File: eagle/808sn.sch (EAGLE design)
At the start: 76 parts, among them IC1 TL072P, IC2 TL072P, Q1 2N3704, Q45 BC546A, Q46 BC556, Q47 BC546A, Q48 BC546A, Q49 BC546A

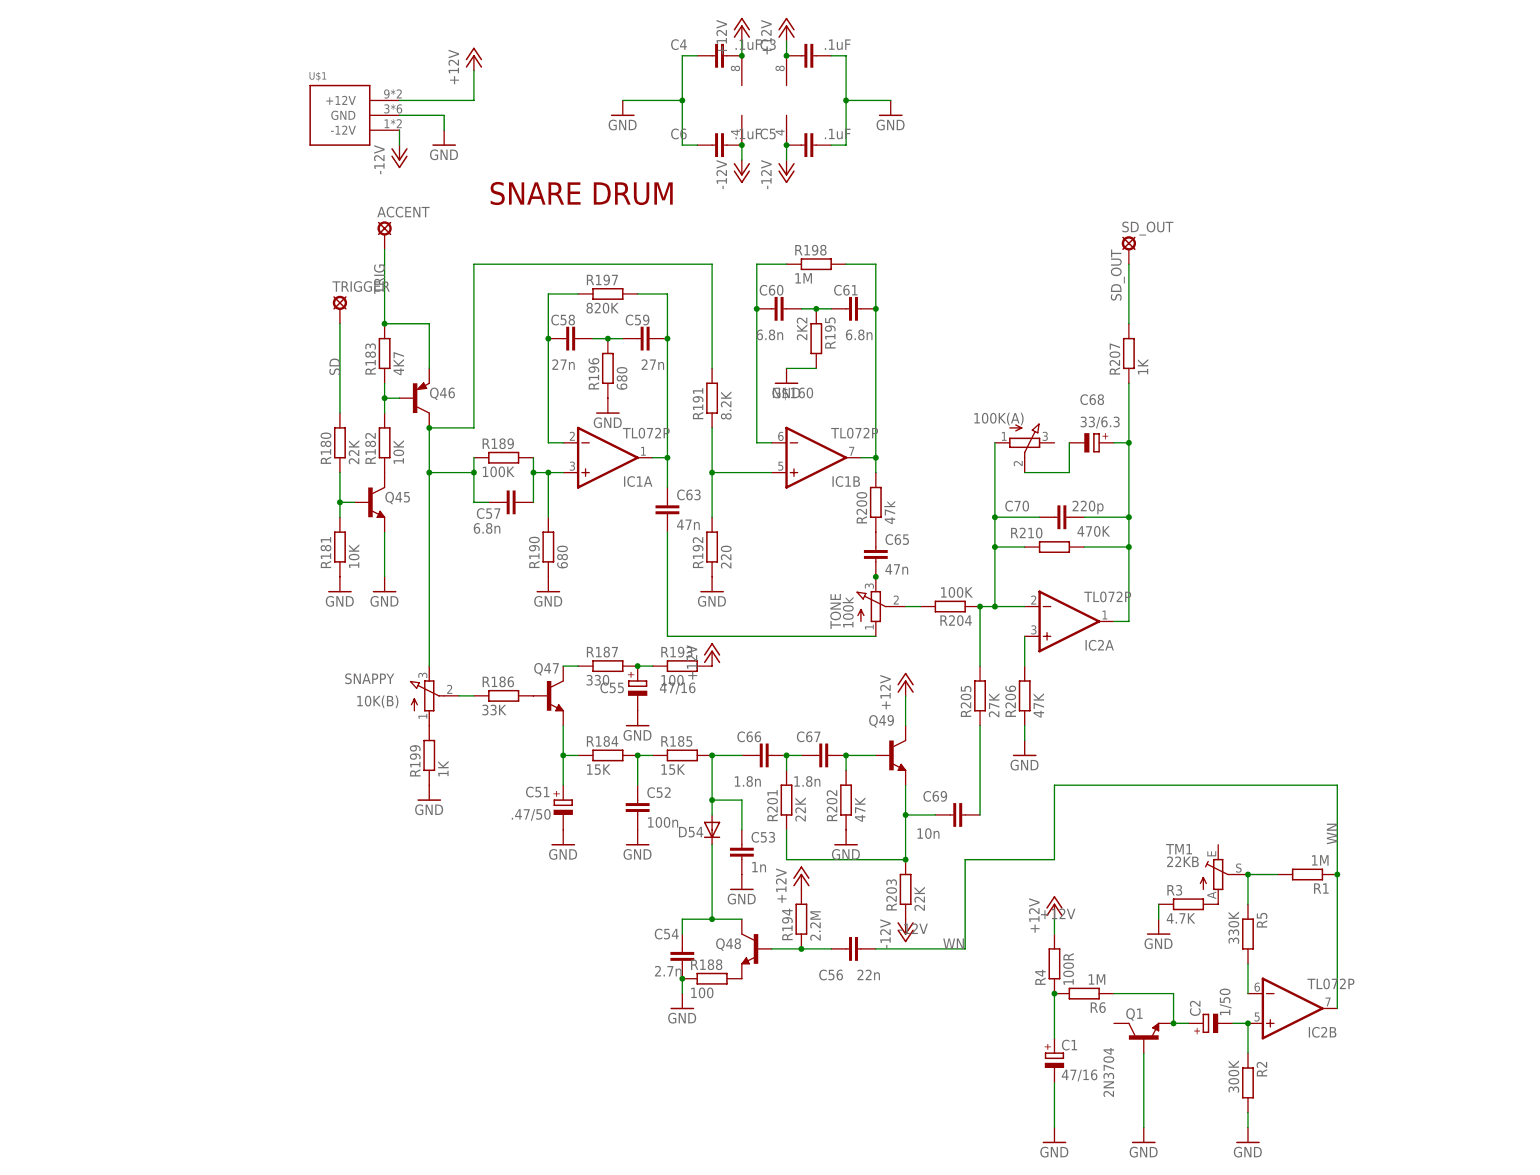
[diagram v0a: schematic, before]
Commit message: updated fittings and replaced with 2n390x
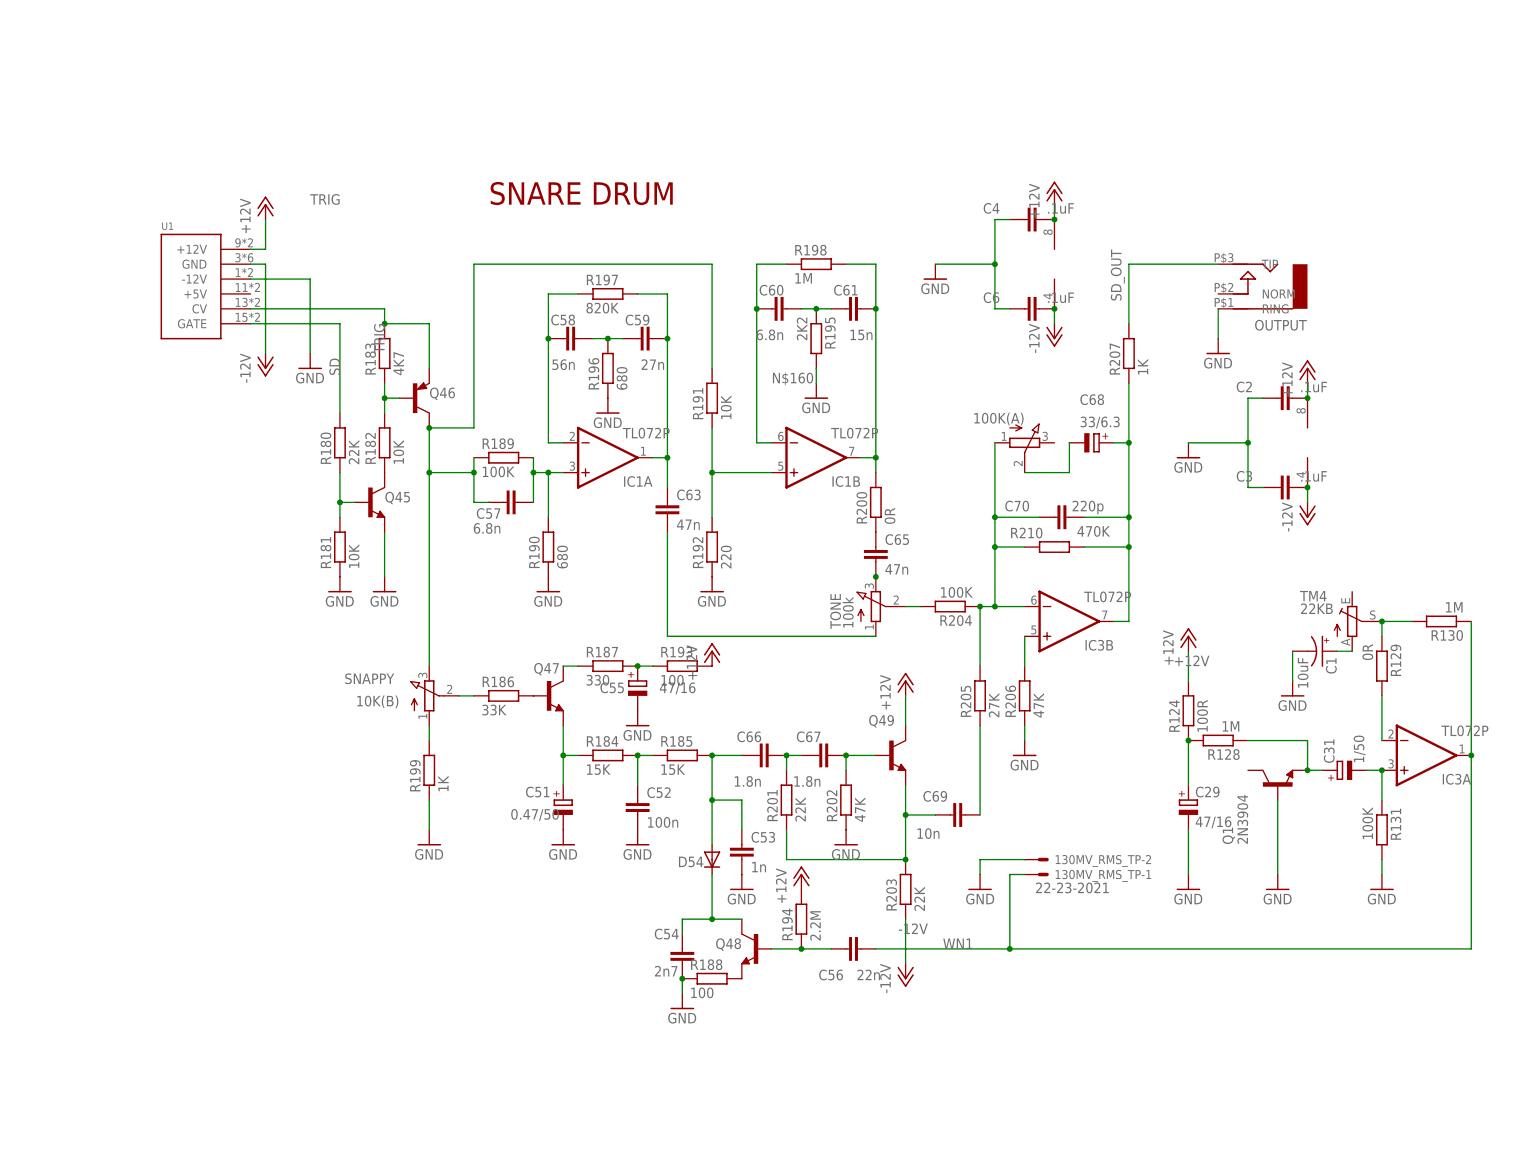
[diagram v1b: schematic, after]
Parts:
- removed ACCENT, SD_OUT, TRIGGER: LSP11, solpad:LSP11
- removed C5: .1uF, TR808clone:C-EU025-025X050
- removed IC2: TL072P, linear:TL072P
- removed R1, R6: 1M, TR808clone:R-EU_0207/5V
- removed R2: 300K, TR808clone:R-EU_0207/5V
- removed R3: 4.7K, TR808clone:R-EU_0207/5V
- removed R4: 100R, TR808clone:R-EU_0207/5V
- removed R5: 330K, TR808clone:R-EU_0207/5V
- removed TM1: 22KB, pot:TRIM_1234-S64YW
- removed U$1: POWER_SIMPLE10, eurorack:POWER_SIMPLE10
- added 130MV_RMS_TP: 22-23-2021, con-molex:22-23-2021
- added C29: 47/16, TR808clone:CPOL-EUE2.5-5
- added C31: 1/50, TR808clone:CPOL-EUE2.5-5
- added IC3: TL072P, linear:TL072P
- added OUTPUT: AUDIO-JACK, erthenvar:AUDIO-JACK
- added R124: 100R, TR808clone:R-EU_0207/7
- added R128, R130: 1M, TR808clone:R-EU_0207/7
- added R129: 0R, TR808clone:R-EU_0207/7
- added R131: 100K, TR808clone:R-EU_0207/7
- added TM4: 22KB, TR808clone:TRIM_EU-B64Y
- added U1: POWER, eurorack:POWER
- C1: value 47/16 -> 10uF; device TR808clone:CPOL-EUE2.5-5 -> rcl:CPOL-USB45181A
- C2: value 1/50 -> .1uF; device TR808clone:CPOL-EUE2.5-5 -> TR808clone:C-EU025-025X050
- C51: value .47/50 -> 0.47/50
- C54: value 2.7n -> 2n7
- C58: value 27n -> 56n
- C61: value 6.8n -> 15n
- Q1: value 2N3704 -> 2N3904; device transistor:2N3704 -> transistor-npn:2N3904
- Q45, Q47, Q48, Q49: value BC546A -> 2N3904; device transistor-npn:BC546A -> 808_lt:2N3904
- Q46: value BC556 -> 2N3906; device transistor-pnp:BC556 -> 808_lt:2N3906
- R191: value 8.2K -> 10K
- R200: value 47k -> 0R
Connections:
- removed net N$2: C2.-, IC2B.+IN, R2.1
- removed net N$707: R1.2, R5.1, TM1.S
- removed net N$709: C2.+, Q1.E, R6.1
- removed net N$710: C1.+, R4.1, R6.2
- removed net N$711: R3.2, TM1.A
- removed net WN: C56.2, IC2B.OUT, R1.1
- new net N$280: C31.-, IC3A.+IN, R131.1
- new net N$4: IC3A.-IN, R129.2
- new net N$490: R129.1, R130.2, TM4.S
- new net N$491: C31.+, Q1.E, R128.1
- new net N$492: C29.+, R124.1, R128.2
- new net WN1: 130MV_RMS_TP-1.S, C56.2, IC3A.OUT, R130.1
- net +12V: now also C2.2, IC3P.V+, R124.2, U1.+12V; no longer C3.1, IC2P.V+, R4.2, U$1.+12V
- net -12V: now also C3.2, IC3P.V-, U1.GND; no longer C5.1, IC2P.V-, U$1.-12V
- net GND: now also 130MV_RMS_TP-2.S, C2.1, C29.-, C3.1, OUTPUT.RING, R131.2, U1.-12V; no longer C3.2, C5.2, R2.2, R3.1, U$1.GND
- net N$1: now also IC3B.+IN; no longer IC2A.+IN
- net N$129: now also IC3B.OUT; no longer IC2A.OUT
- net N$3: now also C1.+, TM4.A; no longer IC2B.-IN, R5.2
- net N$35: now also IC3B.-IN; no longer IC2A.-IN
- net SD: now also U1.GATE; no longer TRIGGER.MP
- net SD_OUT: now also OUTPUT.TIP; no longer SD_OUT.MP
- net TRIG: now also U1.CV; no longer ACCENT.MP
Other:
- moved on the sheet: C1, C3, C4, C6, D54, R199

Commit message: 92pct autorouted
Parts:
- removed U1: POWER, eurorack:POWER
- added ACCENT, GATE: LSP10, solpad:LSP10
- added C5, C7: 10u, rcl:CPOL-USB45181A
- added OUTPUT_NORM: 22-23-2021, con-molex:22-23-2021
- added PWR1: POWER, eurorack:POWER
- added U$1, U$2: FB, adafruit:FB
- R187, R193, R195, R196, R201, R205: device TR808clone:R-EU_0207/5V -> TR808clone:R-EU_0207/7
- R194, R203, R207: device TR808clone:R-EU_0207/5V -> TR808clone:R-EU_0309/10
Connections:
- new net N$10: PWR1.+12V, U$1.1
- new net N$2: OUTPUT.NORM, OUTPUT_NORM-1.S
- new net N$37: PWR1.-12V, U$2.1
- net +12V: now also C5.+, U$1.2; no longer U1.+12V
- net -12V: now also C7.-, U$2.2; no longer U1.GND
- net GND: now also OUTPUT_NORM-2.S; no longer U1.-12V
- net N$26: now also C5.-, C7.+, PWR1.GND
- net SD: now also GATE.MP, PWR1.GATE; no longer U1.GATE
- net TRIG: now also ACCENT.MP, PWR1.CV; no longer U1.CV
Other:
- moved on the sheet: C2, C3, OUTPUT, R207

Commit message: board started over
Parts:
- C52: device TR808clone:C-EU075-032X103 -> TR808clone:C-EU050-045X075
- C6: device TR808clone:C-EU025-025X050 -> TR808clone:C-EU050-025X075
- C69: device TR808clone:C-EU3.5MM_PITCH -> TR808clone:C-EU075-042X103
- R194, R203: device TR808clone:R-EU_0309/10 -> TR808clone:R-EU_0207/7
- R204: device TR808clone:R-EU_0207/5V -> TR808clone:R-EU_0207/7
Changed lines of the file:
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@@
 <part name="R184" library="TR808clone" deviceset="R-EU_" device="0207/5V" value="15K"/>
 <part name="R185" library="TR808clone" deviceset="R-EU_" device="0207/5V" value="15K"/>
-<part name="C52" library="TR808clone" deviceset="C-EU" device="075-032X103" value="100n"/>
+<part name="C52" library="TR808clone" deviceset="C-EU" device="050-045X075" value="100n"/>
 <part name="C55" library="TR808clone" deviceset="CPOL-EU" device="E2-5" value="47/16"/>
 <part name="C51" library="TR808clone" deviceset="CPOL-EU" device="E2-5" value="0.47/50"/>
@@
 <part name="GND13" library="supply1" deviceset="GND" device=""/>
 <part name="GND14" library="supply1" deviceset="GND" device=""/>
-<part name="R203" library="TR808clone" deviceset="R-EU_" device="0309/10" value="22K"/>
+<part name="R203" library="TR808clone" deviceset="R-EU_" device="0207/7" value="22K"/>
 <part name="Q48" library="808_lt" deviceset="2N3904" device=""/>
 <part name="C54" library="TR808clone" deviceset="C-EU" device="3.5MM_PITCH" value="2n7"/>
 <part name="R188" library="TR808clone" deviceset="R-EU_" device="0207/5V" value="100"/>
-<part name="R194" library="TR808clone" deviceset="R-EU_" device="0309/10" value="2.2M"/>
+<part name="R194" library="TR808clone" deviceset="R-EU_" device="0207/7" value="2.2M"/>
 <part name="C56" library="TR808clone" deviceset="C-EU" device="4MM_PITCH" value="22n"/>
 <part name="GND58" library="supply1" deviceset="GND" device=""/>
-<part name="C69" library="TR808clone" deviceset="C-EU" device="3.5MM_PITCH" value="10n"/>
-<part name="R204" library="TR808clone" deviceset="R-EU_" device="0207/5V" value="100K"/>
+<part name="C69" library="TR808clone" deviceset="C-EU" device="075-042X103" value="10n"/>
+<part name="R204" library="TR808clone" deviceset="R-EU_" device="0207/7" value="100K"/>
 <part name="R205" library="TR808clone" deviceset="R-EU_" device="0207/7" value="27K"/>
 <part name="R206" library="TR808clone" deviceset="R-EU_" device="0207/5V" value="47K"/>
@@
 <part name="IC1" library="linear" deviceset="TL072" device="P"/>
 <part name="C4" library="TR808clone" deviceset="C-EU" device="025-025X050" value=".1uF"/>
-<part name="C6" library="TR808clone" deviceset="C-EU" device="025-025X050" value=".1uF"/>
+<part name="C6" library="TR808clone" deviceset="C-EU" device="050-025X075" value=".1uF"/>
 <part name="GND15" library="supply1" deviceset="GND" device=""/>
 <part name="R130" library="TR808clone" deviceset="R-EU_" device="0207/7" value="1M"/>

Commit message: 94pct autorouted
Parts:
- R183, R189: device TR808clone:R-EU_0207/5V -> TR808clone:R-EU_0207/2V
- R186: device TR808clone:R-EU_0207/5V -> TR808clone:R-EU_0309/12
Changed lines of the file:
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@@
 <part name="R181" library="TR808clone" deviceset="R-EU_" device="0207/5V" value="10K"/>
 <part name="R182" library="TR808clone" deviceset="R-EU_" device="0207/5V" value="10K"/>
-<part name="R183" library="TR808clone" deviceset="R-EU_" device="0207/5V" value="4K7"/>
+<part name="R183" library="TR808clone" deviceset="R-EU_" device="0207/2V" value="4K7"/>
 <part name="Q45" library="808_lt" deviceset="2N3904" device=""/>
 <part name="Q46" library="808_lt" deviceset="2N3906" device=""/>
@@
 <part name="C59" library="TR808clone" deviceset="C-EU" device="050-024X044" value="27n"/>
 <part name="C57" library="TR808clone" deviceset="C-EU" device="4MM_PITCH" value="6.8n"/>
-<part name="R189" library="TR808clone" deviceset="R-EU_" device="0207/5V" value="100K"/>
+<part name="R189" library="TR808clone" deviceset="R-EU_" device="0207/2V" value="100K"/>
 <part name="R196" library="TR808clone" deviceset="R-EU_" device="0207/7" value="680"/>
 <part name="R197" library="TR808clone" deviceset="R-EU_" device="0207/5V" value="820K"/>
@@
 <part name="R199" library="TR808clone" deviceset="R-EU_" device="0207/5V" value="1K"/>
 <part name="GND9" library="supply1" deviceset="GND" device=""/>
-<part name="R186" library="TR808clone" deviceset="R-EU_" device="0207/5V" value="33K"/>
+<part name="R186" library="TR808clone" deviceset="R-EU_" device="0309/12" value="33K"/>
 <part name="Q47" library="808_lt" deviceset="2N3904" device=""/>
 <part name="R187" library="TR808clone" deviceset="R-EU_" device="0207/7" value="330"/>

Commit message: routed
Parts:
- C31: device TR808clone:CPOL-EUE2.5-5 -> TR808clone:CPOL-EUE3.5-8
- C51: device TR808clone:CPOL-EUE2-5 -> TR808clone:CPOL-EUE3.5-8
- R184, R185: device TR808clone:R-EU_0207/5V -> TR808clone:R-EU_0207/7
- R189: device TR808clone:R-EU_0207/2V -> TR808clone:R-EU_0207/5V
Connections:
- net GND: now also C5.-, C7.+, PWR1.GND
- net N$26: no longer C5.-, C7.+, PWR1.GND
